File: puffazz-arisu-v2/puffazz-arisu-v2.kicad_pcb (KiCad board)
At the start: 2 copper layers, 339.1 x 118.7 mm, 82 parts, among them SW1 SW_Push, U1 ATmega32U4-AU, Y1 16MHz

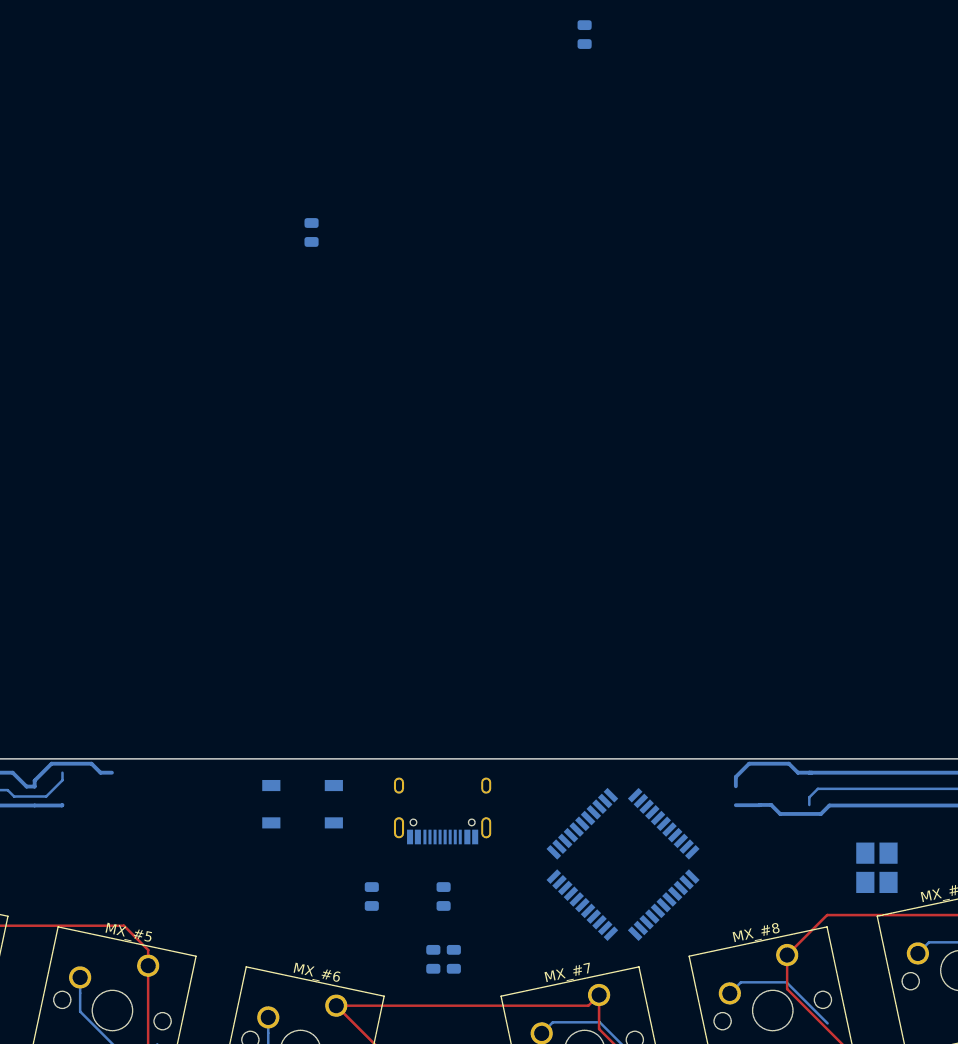
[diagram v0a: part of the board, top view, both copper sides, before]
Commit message: Completed placing all components, missing some 5V routes.
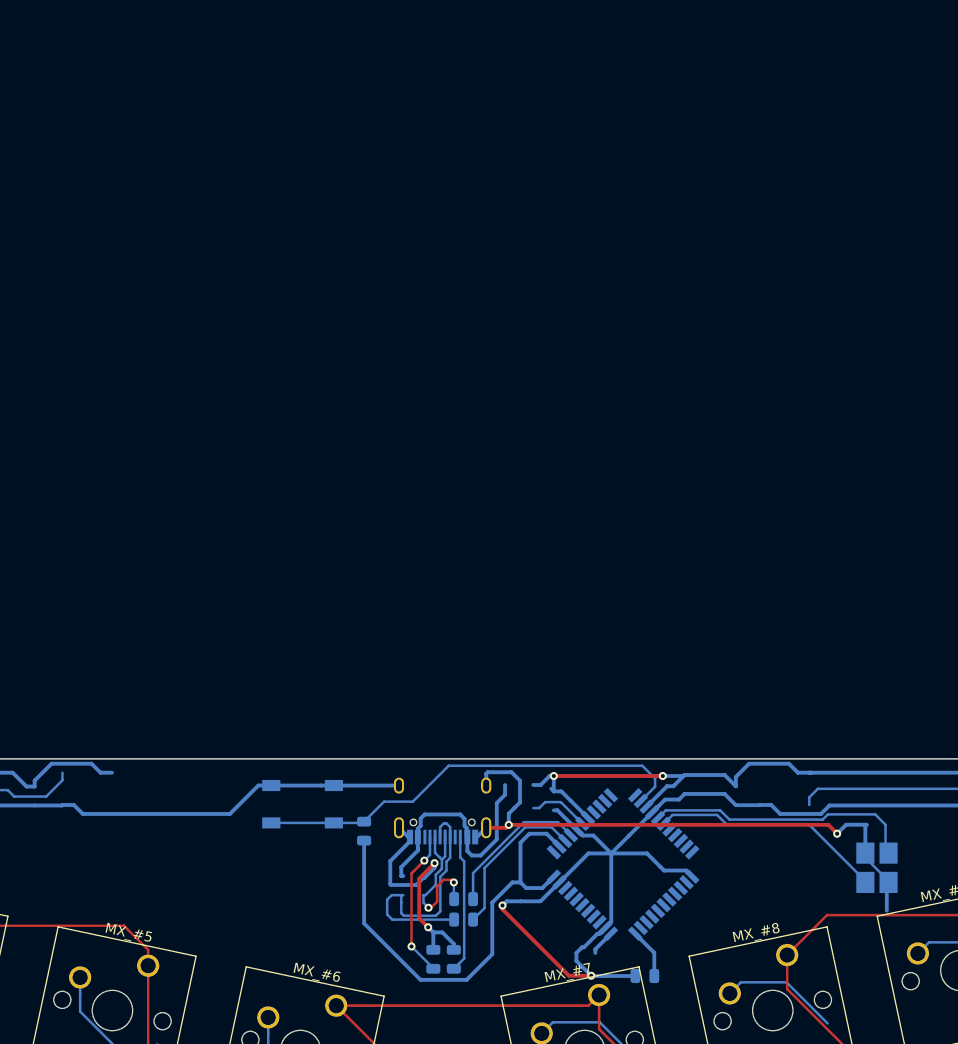
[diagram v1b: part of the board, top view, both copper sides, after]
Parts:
- moved R2 93.5 mm to (205.4, 71.8), turned to 0 degrees
- moved R1 59.5 mm to (177.5, 57.4), turned to 270 degrees
- moved R6 9.38 mm to (187.4, 66.2), turned to 0 degrees
- moved R5 2.00 mm to (187.4, 64.1), turned to 0 degrees
- turned Y1 to 90 degrees
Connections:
- net ROW0 renamed Net-(U1-Pad37)
- net ROW1 renamed Net-(U1-Pad36)
- net ROW2 renamed Net-(U1-Pad32)
- net ROW3 renamed Net-(U1-Pad31)
- net ROW4 renamed Net-(U1-Pad30)
- net ROW5 renamed Net-(U1-Pad29)
- net ROW6 renamed Net-(U1-Pad28)
- net ROW7 renamed Net-(U1-Pad27)
- net ROW8 renamed Net-(U1-Pad26)
- net ROW9 renamed Net-(U1-Pad25)
- U1 pad 10: COL2 -> Net-(U1-Pad10)
- U1 pad 11: COL3 -> Net-(U1-Pad11)
- U1 pad 38: COL4 -> Net-(U1-Pad38)
- U1 pad 39: COL5 -> Net-(U1-Pad39)
- U1 pad 40: COL6 -> Net-(U1-Pad40)
- U1 pad 41: COL7 -> Net-(U1-Pad41)
- U1 pad 8: COL0 -> Net-(U1-Pad8)
- U1 pad 9: COL1 -> Net-(U1-Pad9)
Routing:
- net ROW1: track 0.00 -> 298.3 mm
- net Net-(U1-Pad36): track 298.3 -> 0.00 mm
- net ROW5: track 0.00 -> 298.0 mm
- net Net-(U1-Pad29): track 298.0 -> 0.00 mm
- net ROW0: track 0.00 -> 296.9 mm
- net Net-(U1-Pad37): track 296.9 -> 0.00 mm
- net ROW3: track 0.00 -> 295.0 mm
- net Net-(U1-Pad31): track 295.0 -> 0.00 mm
- net ROW2: track 0.00 -> 291.0 mm
- net Net-(U1-Pad32): track 291.0 -> 0.00 mm
- net ROW4: track 0.00 -> 288.7 mm
- net Net-(U1-Pad30): track 288.7 -> 0.00 mm
- net ROW7: track 0.00 -> 273.5 mm
- net Net-(U1-Pad27): track 273.5 -> 0.00 mm
- net ROW6: track 0.00 -> 247.6 mm
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
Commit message: Finished routing all the components
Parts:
- moved R2 13.8 mm to (192.6, 66.4)
- moved SW1 6.02 mm to (165.5, 55.5)
- moved R1 6.02 mm to (171.6, 58.2)
- moved Y1 5.72 mm to (233.4, 58.3), turned to 180 degrees
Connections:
- U1 pad 18: Net-(U1-Pad18) -> COL7
- U1 pad 19: Net-(U1-Pad19) -> COL6
- U1 pad 20: Net-(U1-Pad20) -> COL5
- U1 pad 21: Net-(U1-Pad21) -> COL4
- U1 pad 26: Net-(U1-Pad26) -> ROW0
- U1 pad 27: Net-(U1-Pad27) -> ROW1
- U1 pad 28: Net-(U1-Pad28) -> ROW2
- U1 pad 29: Net-(U1-Pad29) -> ROW3
- U1 pad 30: Net-(U1-Pad30) -> ROW4
- U1 pad 31: Net-(U1-Pad31) -> ROW5
- U1 pad 32: Net-(U1-Pad32) -> ROW6
- U1 pad 36: Net-(U1-Pad36) -> ROW7
- U1 pad 37: Net-(U1-Pad37) -> ROW8
- U1 pad 38: Net-(U1-Pad38) -> ROW9
- U1 pad 39: Net-(U1-Pad39) -> COL2
- U1 pad 40: Net-(U1-Pad40) -> COL1
- U1 pad 41: Net-(U1-Pad41) -> COL0
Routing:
- net COL7: track 145.6 -> 280.5 mm
- net COL0: track 168.4 -> 300.3 mm
- net ROW9: track 210.9 -> 331.5 mm, vias 0 -> 2
- net ROW8: track 225.1 -> 344.1 mm, vias 0 -> 2
- net ROW6: track 247.6 -> 351.3 mm, vias 0 -> 2
- net ROW7: track 273.5 -> 372.7 mm, vias 0 -> 2
- net COL6: track 118.9 -> 215.0 mm
- net COL1: track 178.6 -> 271.7 mm
- net ROW5: track 298.0 -> 373.7 mm, vias 0 -> 2
- net ROW4: track 288.7 -> 362.7 mm, vias 0 -> 2
- net ROW3: track 295.0 -> 362.8 mm, vias 0 -> 2
- net COL5: track 197.6 -> 252.3 mm
- net ROW2: track 291.0 -> 344.8 mm, vias 0 -> 2
- net COL2: track 198.0 -> 245.8 mm
- net +5V: track 928.6 -> 967.5 mm, vias 2 -> 6
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
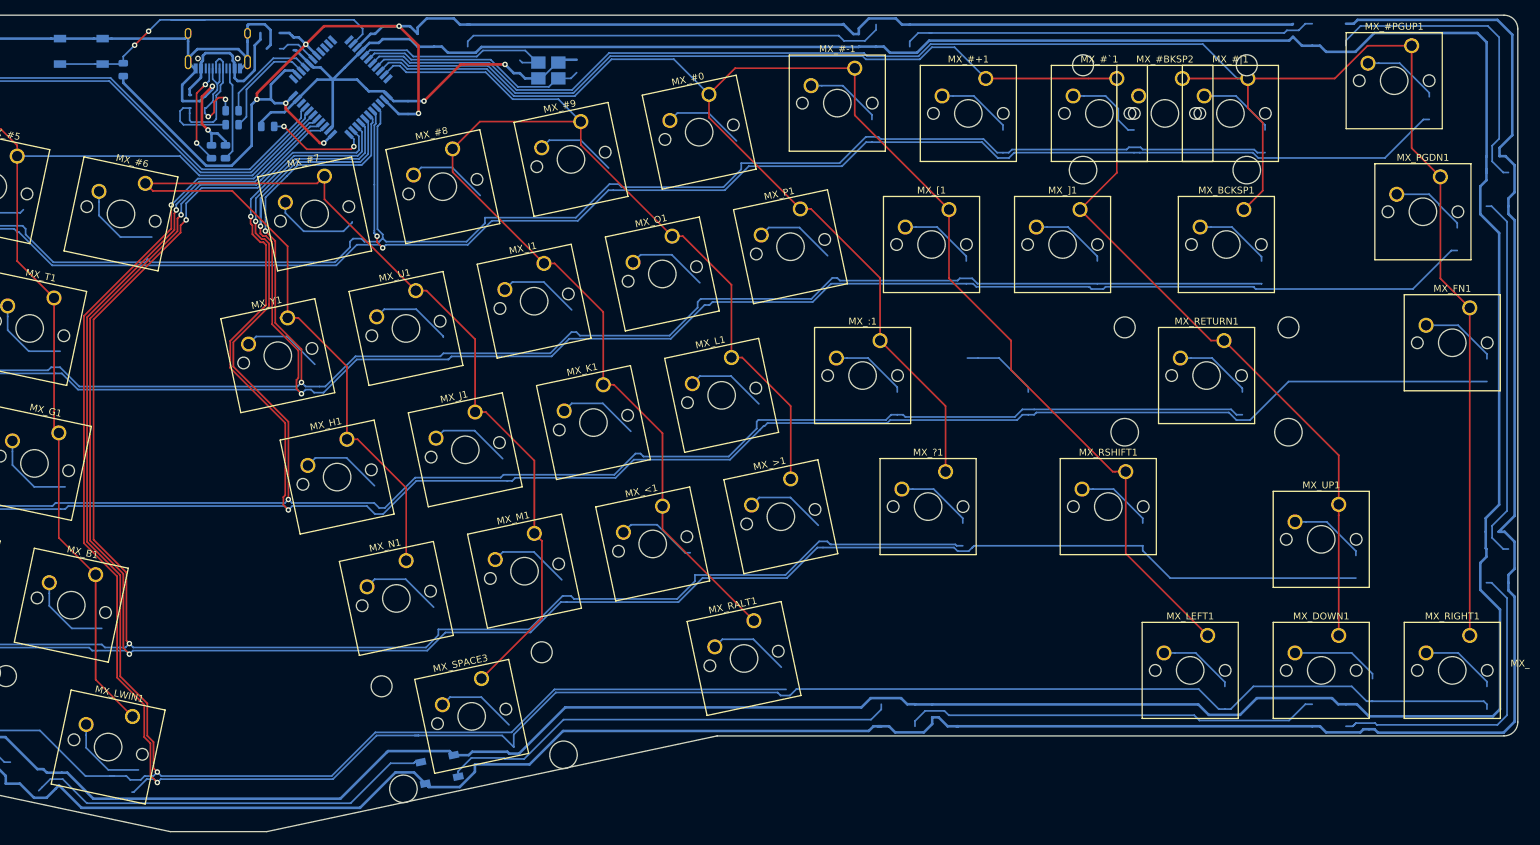
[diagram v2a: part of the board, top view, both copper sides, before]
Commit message: Added ground fills to the MCU, crystal and USB-C port
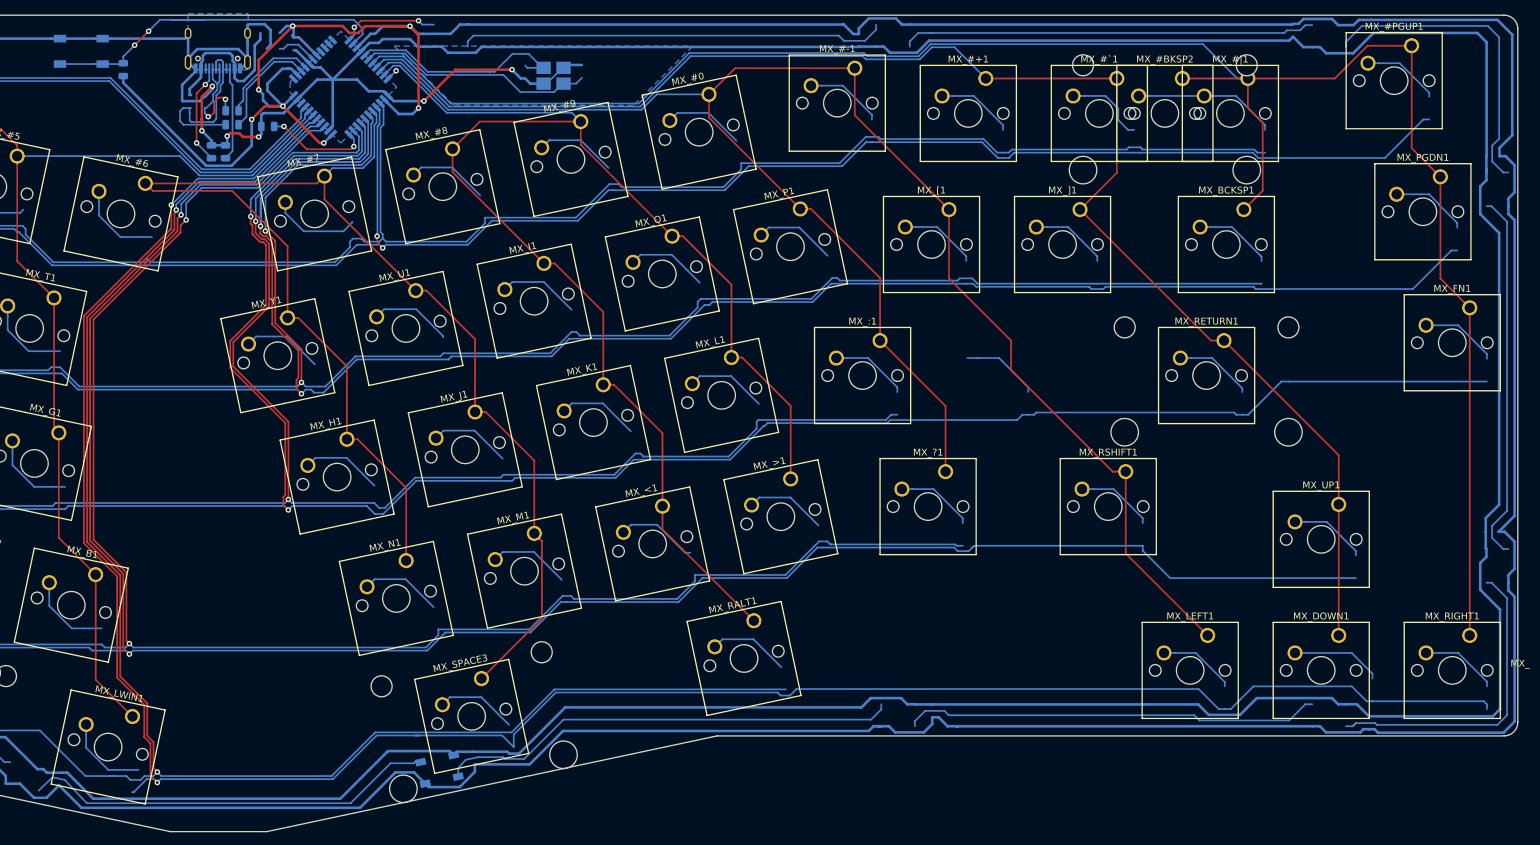
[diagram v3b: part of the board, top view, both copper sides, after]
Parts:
- moved Y1 1.08 mm to (234.1, 59.0)
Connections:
- net Net-(U1-Pad12) renamed RGBLED
- U1 pad 25: Net-(U1-Pad25) -> ROW0
- U1 pad 26: ROW0 -> ROW1
- U1 pad 27: ROW1 -> COL3
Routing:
- net ROW4: track 362.7 -> 311.6 mm
- net +5V: track 967.5 -> 985.1 mm, vias 6 -> 7
- net COL3: track 198.3 -> 213.8 mm
- net RGBLED: track 0.00 -> 14.4 mm, vias 0 -> 2
- net Net-(D9-Pad2): track 11.3 -> 20.8 mm
- net GND: track 986.8 -> 995.8 mm, vias 4 -> 6
- net COL5: track 252.3 -> 249.7 mm
- net Net-(C2-Pad1): track 30.5 -> 33.0 mm
- net Net-(U1-Pad22): track 0.00 -> 1.68 mm, vias 0 -> 1
- net COL6: track 215.0 -> 216.7 mm
- net COL7: track 280.5 -> 282.2 mm
- net Net-(C1-Pad1): track 33.5 -> 34.6 mm
- net ROW5: track 373.7 -> 373.1 mm
- added copper zone on B.Cu, net GND
